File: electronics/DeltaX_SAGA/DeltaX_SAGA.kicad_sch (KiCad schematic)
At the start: 40 parts

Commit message: initial schematic updated
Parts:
- added C?: 10uF, symbol Device:C
- added C?: 1uF, symbol Device:C
- added D?: LED, symbol Device:LED
- added J?: Motor3_Encoder, symbol Connector_Generic:Conn_02x02_Counter_Clockwise
- added J?: Motor2_Encoder, symbol Connector_Generic:Conn_02x02_Counter_Clockwise
- added J?: Motor3_OUT, symbol Connector_Generic:Conn_01x02
- added J?: Servo, symbol Connector_Generic:Conn_02x02_Counter_Clockwise
- added J?: Motor1_OUT, symbol Connector_Generic:Conn_01x02
- added J?: Thrower, symbol Connector_Generic:Conn_02x02_Counter_Clockwise
- added J?: Motor2_OUT, symbol Connector_Generic:Conn_01x02
- added J?: Motor1_Encoder, symbol Connector_Generic:Conn_02x02_Counter_Clockwise
- added R?: R1, symbol Device:R
- added R?: 1k5, symbol Device:R
- added R?: R2, symbol Device:R
- added U?: NCP164C, symbol NCP164C:NCP164C
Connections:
- net +3V3: now also C?.1, D?.2 (A), J?.1 (Pin_1), J?.1 (Pin_1), J?.1 (Pin_1); no longer C?.1, C?.1, C?.2, C?.2, J?.2 (Pin_2), R?.2, U?.15 (GNDB), U?.15 (GNDB), U?.2 (GND), U?.6 (GND), U?.6 (GND), U?.6 (GND), U?.9 (GNDB), U?.9 (GNDB)
- net +5V: no longer C?.1, R?.1, U?.5 (OUT)
- net Thrower_PWM: now also J?.4 (Pin_4)
- net V+: now also J?.1 (Pin_1)
- net Motor2_OUT2: now reaches U?.5 (OUT2)
- net Motor2_OUT2: now also U?.5 (OUT2), J?.1 (Pin_1)
- net Motor2_OUT1: now reaches U?.7 (OUT1)
- net Motor2_OUT1: now also U?.7 (OUT1), J?.2 (Pin_2)
- net Motor1_OUT2: now reaches U?.5 (OUT2)
- net Motor1_OUT2: now also J?.1 (Pin_1)
- net Motor1_OUT1: now reaches U?.7 (OUT1)
- net Motor1_OUT1: now also J?.2 (Pin_2)
- new net: R?.1, U?.5 (OUT)
- new net: R?.1, R?.2, U?.4 (NC/ADJ)
- new net: C?.1, U?.15 (GNDB), U?.9 (GNDB)
- new net: D?.1 (K), R?.1
- new net +5VA: C?.1, C?.1, J?.1 (Pin_1), R?.1, U?.1 (IN), U?.5 (OUT)
- new net GND2: C?.1, C?.2, C?.2, C?.2, C?.2, J?.2 (Pin_2), J?.2 (Pin_2), J?.2 (Pin_2), J?.2 (Pin_2), J?.2 (Pin_2), J?.2 (Pin_2), R?.2, R?.2, R?.2, U?.15 (GNDB), U?.2 (GND), U?.2 (GND), U?.6 (GND), U?.6 (GND), U?.6 (GND), U?.9 (GNDB)
- new net Motor1_EncA: J?.4 (Pin_4)
- new net Motor1_EncB: J?.3 (Pin_3)
- new net Motor2_EncA: J?.4 (Pin_4)
- new net Motor2_EncB: J?.3 (Pin_3)
- new net Motor3_EncA: J?.4 (Pin_4)
- new net Motor3_EncB: J?.3 (Pin_3)
- new net Motor3_OUT1: J?.2 (Pin_2)
- new net Motor3_OUT2: J?.1 (Pin_1)
- new net Servo_PWM: J?.4 (Pin_4)
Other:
- note added: "5V to 3.3V Converter"
- note added: "Motor Encoder Connectors"
- note added: "Motor Ouput Connectors"
- note added: "Thrower & Servo"
- moved on the sheet: C?, FB?, J?, R?, SW?, U?, Y?

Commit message: schematic updated
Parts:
- removed J?: CLk/IO Pins, symbol Connector:Conn_01x04_Male
- removed R?: 10k, symbol Device:R
- removed SW?: SW_SPDT, symbol Switch:SW_SPDT
- added C? (x3): 0.1uF, symbol Device:C
- added D? (x3): LED, symbol Device:LED
- added J?: Servo Power, symbol Connector_Generic:Conn_01x02
- added J?: Thrower Power, symbol Connector_Generic:Conn_01x02
- added J?: Programmer, symbol Connector_Generic:Conn_02x05_Odd_Even
- added R? (x4): 1k5, symbol Device:R
- added U?: CM1223, symbol CM1223:CM1223
- added U?: MAX12930, symbol MAX12930:MAX12930
- J?: value Servo -> Servo Signal
- J?: value Thrower -> Thrower Signal
- R?: value R1 -> 200k
- R?: value R2 -> 100k
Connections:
- net +3V3: now also J?.6 (Shield), J?.1 (Pin_1), R?.1, U?.1 (VDDA), U?.2 (Vn), U?.4 (GNDA), U?.8 (VDDB); no longer U?.2 (GNDA), U?.2 (GNDA)
- net +5V: now also U?.1 (Vp)
- net +5VA: now also J?.1 (Pin_1); no longer J?.1 (Pin_1)
- net GND2: now also C?.2, C?.2, C?.2, J?.2 (Pin_2), J?.2 (Pin_2), J?.3 (Pin_3), J?.5 (Pin_5), J?.9 (Pin_9), R?.1, R?.1, R?.1, U?.5 (GNDB); no longer U?.15 (GNDB)
- net NRST: now also J?.10 (Pin_10)
- net Thrower_PWM: now also J?.3 (Pin_3); no longer J?.4 (Pin_4)
- net USB_D+: now also R?.2, U?.4 (CH2)
- net USB_D-: now also U?.3 (CH1)
- net V+: now also C?.1, C?.1, C?.1, J?.1 (Pin_1); no longer J?.1 (Pin_1)
- net nSLEEP: now reaches U?.3 (nSLEEP)
- net nSLEEP: now also U?.3 (nSLEEP), U?.3 (nSLEEP), U?.5 (INA3)
- net at C?.1, U?.9 (GNDB): no longer U?.15 (GNDB)
- net servoPWM_Isolated: now reaches J?.3 (Pin_3)
- net servoPWM_Isolated: now also U?.7 (OUT1)
- net BOOT0: no longer names the net of U?.31 (PG8-BOOT0)
- net Servo_PWM: no longer names the net of J?.4 (Pin_4)
- removed net nFault: U?.1 (nFAULT), U?.1 (nFAULT), U?.1 (nFAULT), U?.5 (INA3)
- net nFault_Isolated renamed nSLEEP_Isolated
- new net: D?.2 (A), U?.1 (nFAULT) (x3)
- new net: D?.1 (K), R?.2 (x3)
- new net SWCLK: J?.4 (Pin_4)
- new net SWDIO: J?.2 (Pin_2)
- new net servoPWM: U?.2 (IN1)
- no-connect marks 2 -> 1
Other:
- note added: "Programmer Connector"
- note added: "Servo"
- note added: "Thrower Motor"
- note removed: "CLK/IO Header Pins"
- note removed: "Thrower & Servo"
- note removed: "uC Switch"
- moved on the sheet: C?, J?, R?, U?, Y?

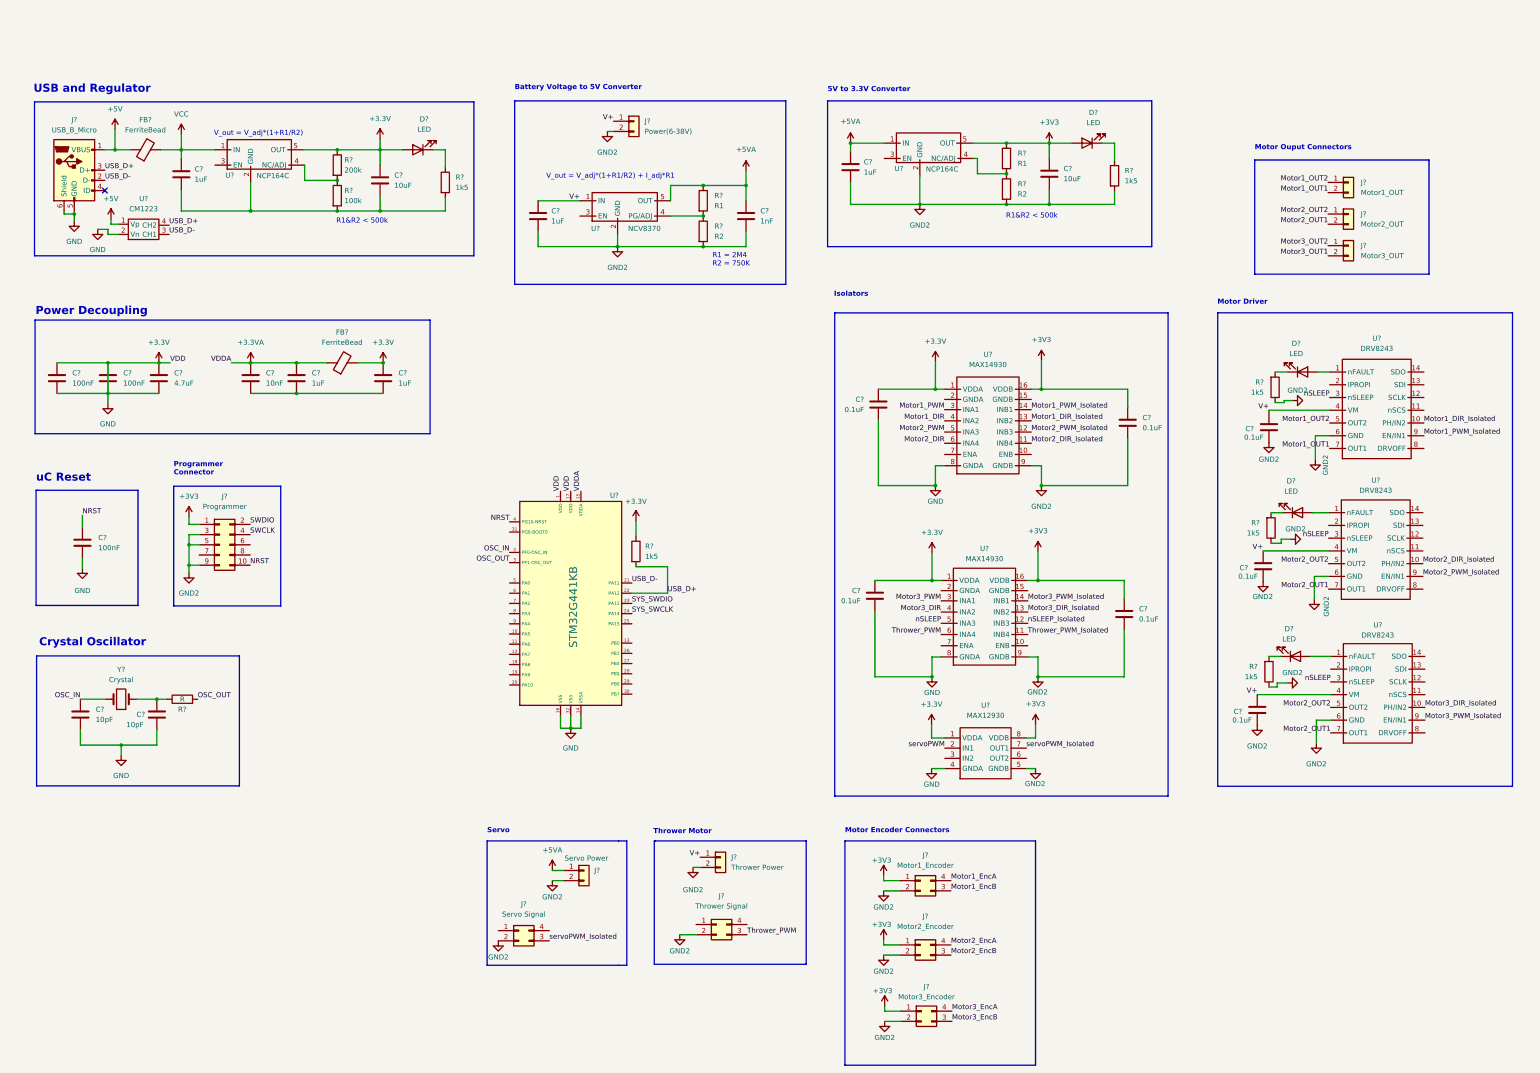
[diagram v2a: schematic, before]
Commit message: schematic annotated and some components assigned
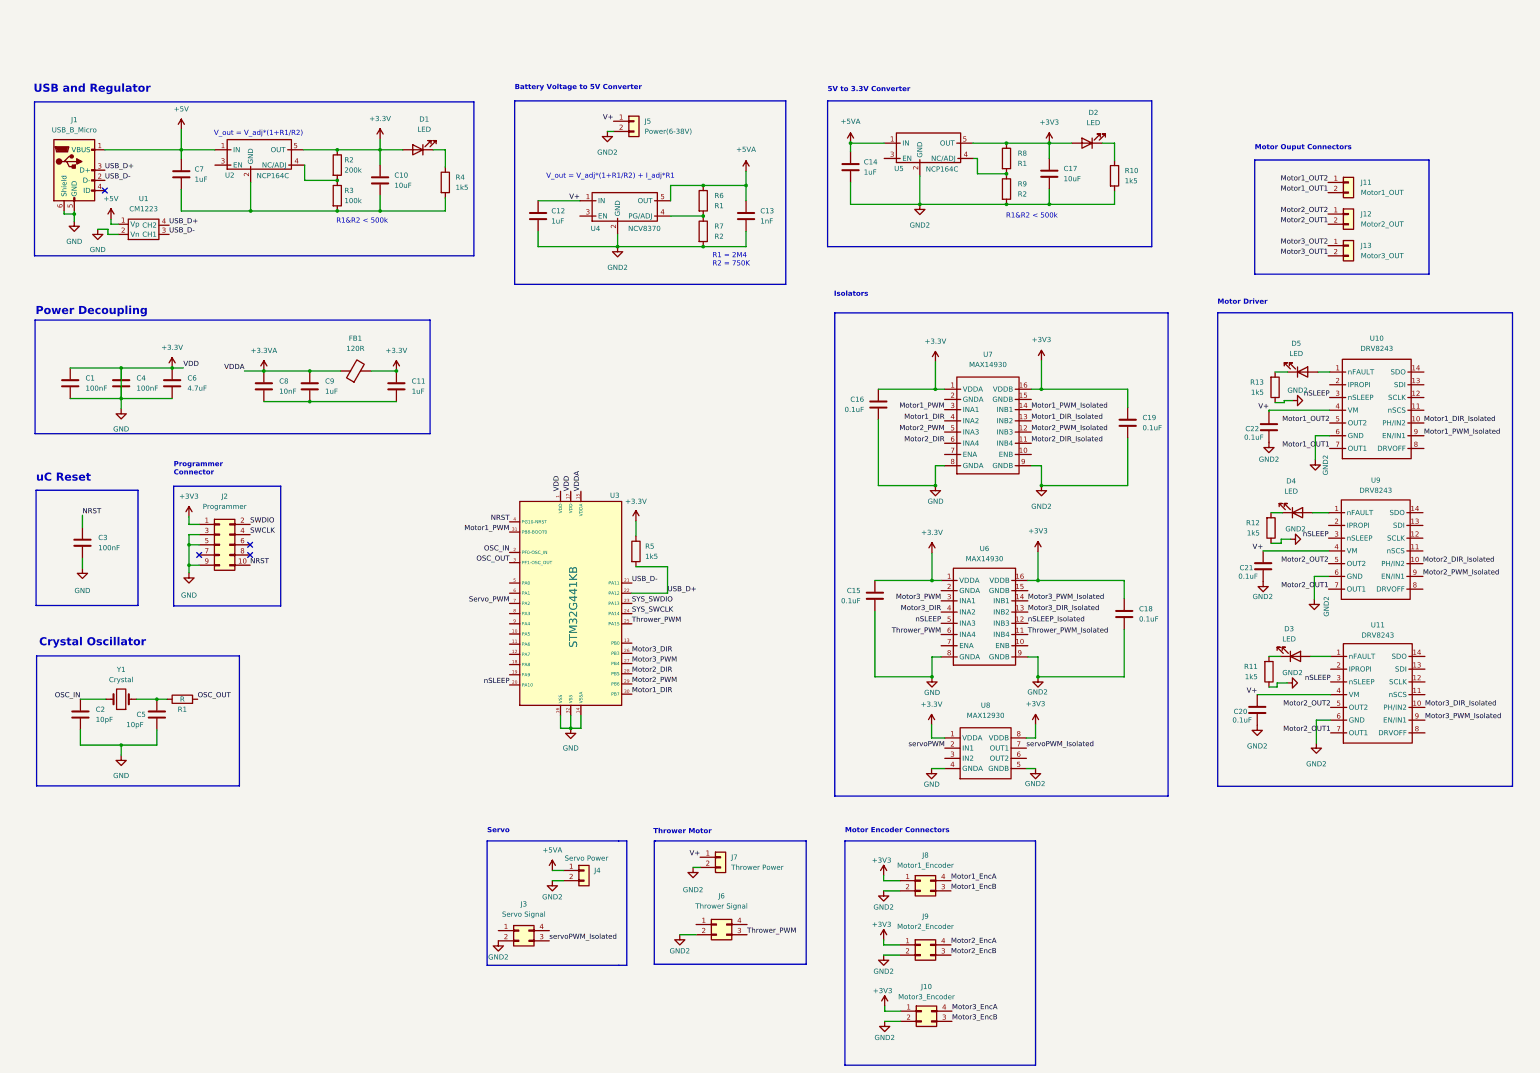
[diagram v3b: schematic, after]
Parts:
- removed FB?: FerriteBead, symbol Device:FerriteBead
- C1, C11, C12, C13, C14, C15, C16, C18, C19, C2, C20, C21, C22, C3, C4, C5, C7, C8, C9: renamed from C?; footprint (none) -> Capacitor_SMD:C_0402_1005Metric
- C10, C17, C6: renamed from C?; footprint (none) -> Capacitor_SMD:C_0603_1608Metric
- D1, D2, D3, D4, D5: renamed from D?; footprint (none) -> LED_SMD:LED_0603_1608Metric
- FB1: renamed from FB?; value FerriteBead -> 120R; footprint (none) -> Inductor_SMD:L_0603_1608Metric
- J1: renamed from J?; footprint (none) -> Connector_USB:USB_Micro-B_Amphenol_10118194_Horizontal
- J11, J12, J13, J5, J7: renamed from J?; footprint (none) -> Connector_PinHeader_1.00mm:PinHeader_1x02_P1.00mm_Vertical_SMD_Pin1Right
- R1, R10, R11, R12, R13, R2, R3, R4, R5, R6, R7, R8, R9: renamed from R?; footprint (none) -> Resistor_SMD:R_0402_1005Metric
- gave numbers to parts that had none: 19
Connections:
- net VCC is gone; now on net +5V: C7.1, U2.1 (IN)
- net +3V3: now also J2.3 (Pin_3), J2.5 (Pin_5), J2.9 (Pin_9)
- net GND2: no longer J2.3 (Pin_3), J2.5 (Pin_5), J2.9 (Pin_9)
- net Motor1_DIR: now also U3.30 (PB7)
- net Motor1_PWM: now also U3.31 (PB8-BOOT0)
- net Motor2_DIR: now also U3.28 (PB5)
- net Motor2_PWM: now also U3.29 (PB6)
- net Motor3_DIR: now also U3.26 (PB3)
- net Motor3_PWM: now also U3.27 (PB4)
- net Thrower_PWM: now also U3.25 (PA15)
- net nSLEEP: now also U3.20 (PA10)
- net Servo_PWM: now reaches U3.7 (PA2)
- no-connect marks 1 -> 4
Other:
- moved on the sheet: C1, C11, C4, C6, C8, C9, FB1

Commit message: updated the boardc schematic and pcb design
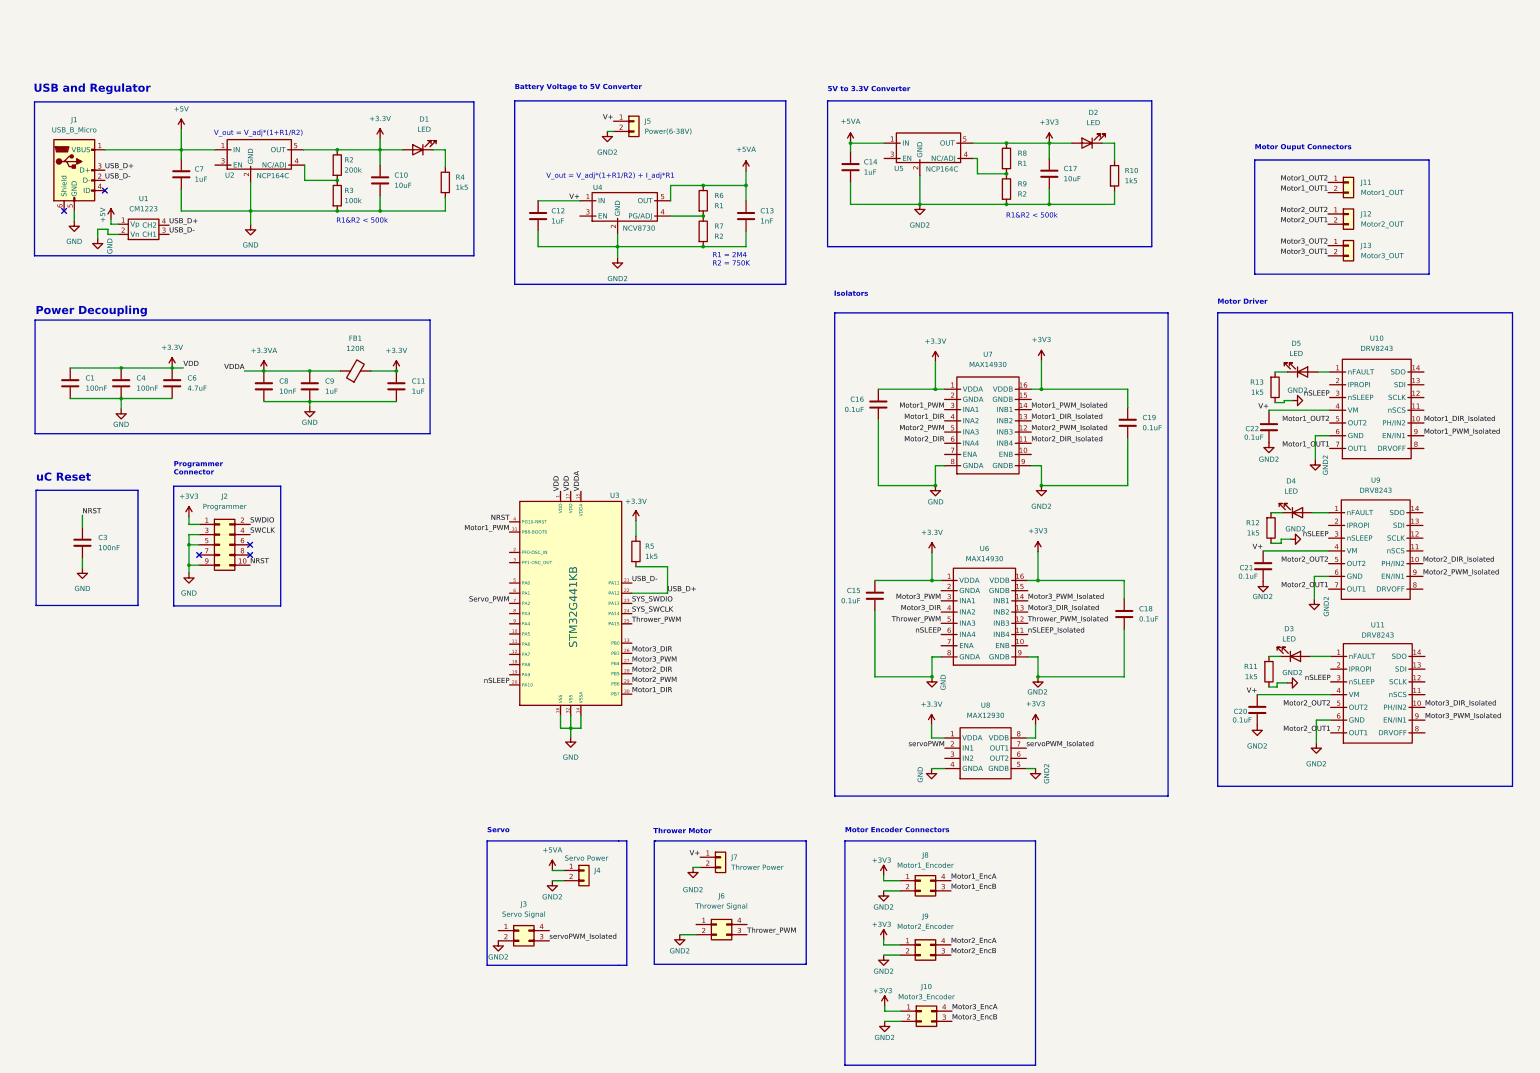
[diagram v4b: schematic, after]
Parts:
- removed C2, C5: 10pF, Capacitor_SMD:C_0402_1005Metric, symbol Device:C
- removed R1: R, Resistor_SMD:R_0402_1005Metric, symbol Device:R
- removed U4: NCV8370, symbol NCV8370:NCV8370
- removed Y1: Crystal, symbol Device:Crystal
- added U4: NCV8730, NCV8730:SOT95P275X110-5N, symbol NCV8730:NCV8730
- J1: footprint Connector_USB:USB_Micro-B_Amphenol_10118194_Horizontal -> USB_Amphenol:FCI_10118193-0001LF
- J10, J3, J6, J8, J9: footprint (none) -> Micro-MaTch215079-4:TE_7-215079-4
- J2: footprint (none) -> Samtec FTSH-105-01-L-DV-K:SAMTEC_FTSH-105-XX-X-DV
- J4: footprint (none) -> Connector_PinSocket_2.54mm:PinSocket_1x02_P2.54mm_Vertical_SMD_Pin1Right
- U1: footprint (none) -> CM1223:SOT192P237X122-4N
- U10, U11, U9: footprint (none) -> DRV8243:DRV8243
- U2, U5: footprint (none) -> NCP164C:SOP95P275X110-5N
- U3: footprint (none) -> STM32G441KB:STM32G441KB
- U6, U7: footprint (none) -> MAX14930:MAX14930DASE+
- U8: footprint (none) -> MAX12930:MAX12930EASA+
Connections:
- net +3V3: no longer C1.2, C15.1, C16.1, C3.2, C4.2, C6.2, J1.5 (GND), J1.6 (Shield), J2.3 (Pin_3), J2.5 (Pin_5), J2.9 (Pin_9), U1.2 (Vn), U3.14 (VSSA), U3.16 (VSS), U3.32 (VSS), U6.8 (GNDA), U7.8 (GNDA), U8.4 (GNDA)
- net +5VA: now also U4.5 (OUT)
- net GND2: now also U4.2 (GND)
- net Thrower_PWM: now also U6.5 (INA3); no longer U6.6 (INA4)
- net Thrower_PWM_Isolated: now also U6.12 (INB3); no longer U6.11 (INB4)
- net V+: now also U4.1 (IN)
- net nSLEEP: now also U6.6 (INA4); no longer U6.5 (INA3)
- net nSLEEP_Isolated: now also U6.11 (INB4); no longer U6.12 (INB3)
- net GND: now reaches C10.2, C7.2, R3.2, R4.2, U2.2 (GND)
- net GND: now also C1.2, C11.2, C15.1, C16.1, C3.2, C4.2, C6.2, C8.2, C9.2, J1.5 (GND), J2.3 (Pin_3), J2.5 (Pin_5), J2.9 (Pin_9), U1.2 (Vn), U3.14 (VSSA), U3.16 (VSS), U3.32 (VSS), U6.8 (GNDA), U7.8 (GNDA), U8.4 (GNDA)
- net at R6.2, R7.1: now also U4.4 (PG/ADJ)
- net OSC_IN: no longer names the net of U3.2 (PF0-OSC_IN)
- net OSC_OUT: no longer names the net of U3.3 (PF1-OSC_OUT)
- no-connect marks 4 -> 5
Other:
- note removed: "Crystal Oscillator"
